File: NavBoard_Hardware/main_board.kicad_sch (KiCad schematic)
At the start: 1 part, among them J1 24Pin_To_16Pin_2.54mm_Separat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

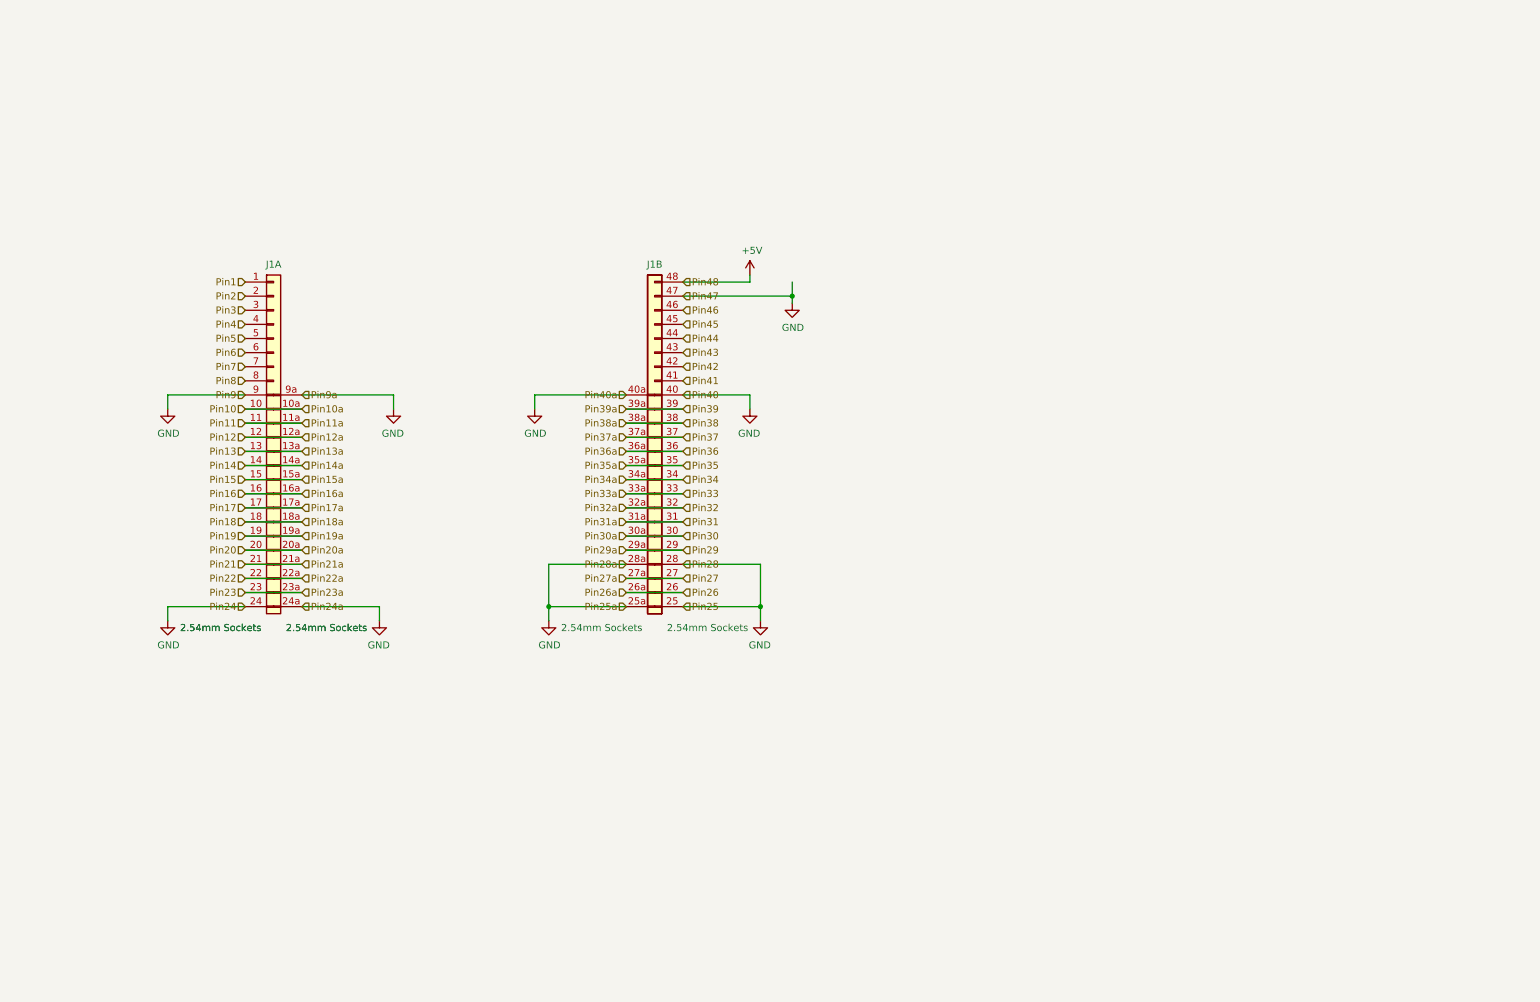
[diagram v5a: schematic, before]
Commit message: Realized this could all fit on a single board
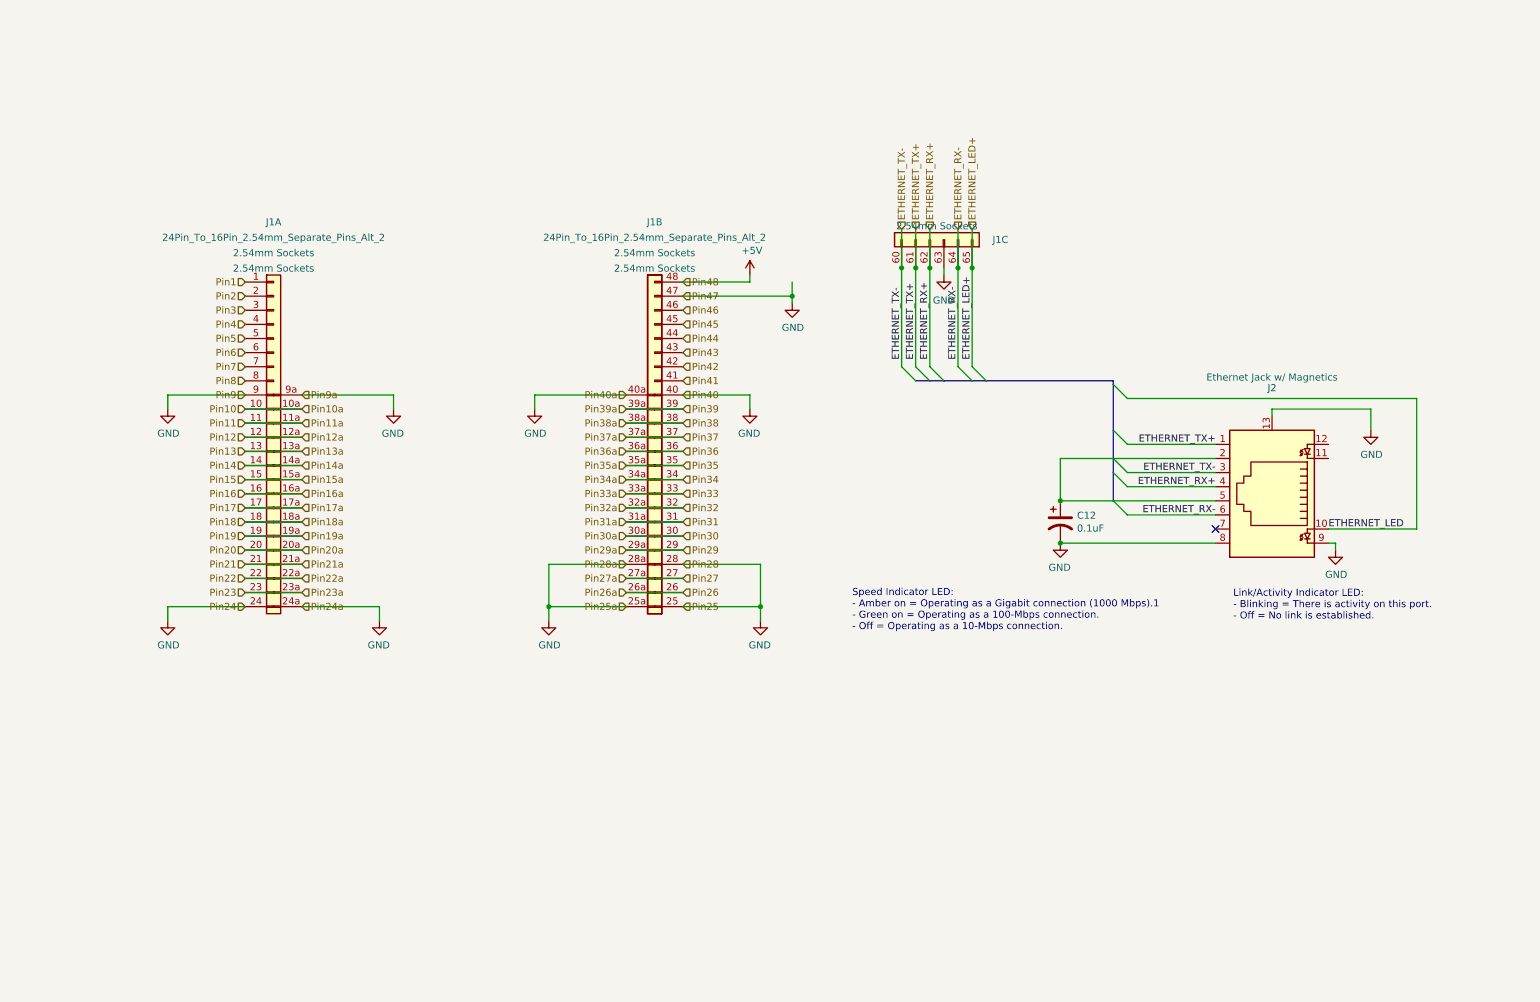
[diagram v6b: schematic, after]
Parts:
- added C12: 0.1uF, Capacitor_SMD:C_0603_1608Metric_Pad1.08x0.95mm_HandSolder, symbol Device:C_Polarized_US
- added unit 3 of J1
- added J2: Ethernet Jack w/ Magnetics, Connector_RJ:RJ45_Cetus_J1B1211CCD_Horizontal, symbol Connector:8P8C_LED_Shielded
- J1: now left out of the parts list
- J1: Field5 2.54mm Sockets -> (none); Inner Headers 2.54mm Sockets -> (none); now left out of the parts list
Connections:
- net GND: now also C12.2, J1.63, J2.13, J2.8, J2.9
- new net: C12.1, J2.2, J2.5
- new net ETHERNET_LED: J2.10
- new net ETHERNET_LED+: J1.65
- new net ETHERNET_RX+: J1.62, J2.4
- new net ETHERNET_RX-: J1.64, J2.6
- new net ETHERNET_TX+: J1.61, J2.1
- new net ETHERNET_TX-: J1.60, J2.3
- no-connect marks 0 -> 1
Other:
- note added: "Link/Activity Indicator LED: - Blinking = There is activity on this port. - Off = No link is established."
- note added: "Speed Indicator LED: - Amber on = Operating as a Gigabit connection (1000 Mbps).1 - Green on = Operating as a 100-Mbps connection. - Off = Operating as a 10-Mbps connection."
